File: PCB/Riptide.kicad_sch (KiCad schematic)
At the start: 180 parts, among them SW1 SW_Push, SW10 SW_Push, SW11 SW_Push, SW12 SW_Push, SW13 SW_Push, SW14 SW_Push, SW15 SW_Push, SW16 SW_Push, SW17 SW_Push, SW18 SW_Push, SW19 SW_Push, SW2 SW_Push, SW20 SW_Push, SW21 SW_Push, SW22 SW_Push, SW23 SW_Push, SW24 SW_Push, SW25 SW_Push, SW26 SW_Push, SW27 SW_Push, SW28 SW_Push, SW29 SW_Push, SW3 SW_Push, SW30 SW_Push, SW31 SW_Push, SW32 SW_Push, SW33 SW_Push, SW34 SW_Push, SW35 SW_Push, SW36 SW_Push, SW37 SW_Push, SW38 SW_Push, SW39 SW_Push, SW4 SW_Push, SW40 SW_Push, SW41 SW_Push, SW42 SW_Push, SW43 SW_Push, SW44 SW_Push, SW45 SW_Push, SW46 SW_Push, SW47 SW_Push, SW48 SW_Push, SW49 SW_Push, SW5 SW_Push, SW50 SW_Push, SW51 SW_Push, SW52 SW_Push, SW53 SW_Push, SW54 SW_Push, SW55 SW_Push, SW56 SW_Push, SW57 SW_Push, SW58 SW_Push, SW59 SW_Push, SW6 SW_Push, SW60 SW_Push, SW61 SW_Push, SW62 SW_Push, SW63 SW_Push, SW64 SW_Push, SW65 SW_Push, SW66 SW_Push, SW67 SW_Push, SW68 SW_Push, SW69 SW_Push, SW7 SW_Push, SW70 SW_Push, SW71 SW_Push, SW72 SW_Push, SW73 SW_Push, SW74 SW_Push, SW75 SW_Push, SW76 SW_Push, SW77 SW_Push, SW78 SW_Push, SW79 SW_Push, SW8 SW_Push, SW80 SW_Push, SW81 SW_Push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

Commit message: Finally Done!!
I have been working on this off and on since the 1st lol
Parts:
- removed D63, D64, D65, D66, D67, D69, D70, D71, D72, D77, D78, D80, D81, D82, D83, D84, D86, D87, D88, D89, D90: D, symbol Device:D
- removed SW12, SW18, SW34, SW50, SW61, SW65, SW66, SW67, SW68, SW69, SW73, SW74, SW75, SW76, SW77, SW81, SW82, SW83, SW84, SW85, SW86, SW87, SW88, SW89, SW90: SW_Push, symbol Switch:SW_Push_45deg
- added A1: RaspberryPi_Pico, Module:RaspberryPi_Pico_Common_Unspecified, symbol MCU_Module:RaspberryPi_Pico
- added D102, D105, D106, D115, D116, D117, D118, D119, D120, D121, D122, D123, D124, D97, D98, D99: D, Diode_THT:D_DO-35_SOD27_P7.62mm_Horizontal, symbol Device:D
- added H1, H10, H11, H12, H13, H14, H2, H3, H4, H5, H6, H7, H8, H9: X6511FRS-05-C85D30, Custom:HDR-SMD_5P-P2.54-H-F_X6511FRS-19-C85D30, symbol LCSC Custom:X6511FRS-05-C85D30
- added LED1, LED10, LED11, LED12, LED13, LED14, LED15, LED16, LED17, LED18, LED19, LED2, LED20, LED21, LED22, LED23, LED24, LED25, LED26, LED27, LED28, LED29, LED3, LED30, LED31, LED32, LED33, LED34, LED35, LED36, LED37, LED38, LED39, LED4, LED40, LED41, LED42, LED43, LED44, LED45, LED46, LED47, LED48, LED49, LED5, LED50, LED51, LED52, LED53, LED54, LED55, LED56, LED57, LED58, LED59, LED6, LED60, LED61, LED7, LED8, LED9: SK6812MINI, Custom:LED_SK6812MINI_PLCC4_3.5x3.5mm_P1.75mm, symbol LED:SK6812MINI
- added R1, R2: 4.7K, Resistor_THT:R_Axial_DIN0204_L3.6mm_D1.6mm_P5.08mm_Horizontal, symbol Device:R
- added SW14, SW15, SW16, SW22, SW23, SW24, SW31, SW38, SW39, SW40, SW46, SW48, SW54, SW55, SW7, SW8: SW_Push, Custom Keyboard Parts:SW_Cherry_MX_PCB_1.00u, symbol Switch:SW_Push_45deg
- added SW30: SW_Push, Custom Keyboard Parts:SW_Cherry_MX_PCB_2.00u, symbol Switch:SW_Push_45deg
- added SW32: SW_Push, Custom Keyboard Parts:SW_Cherry_MX_PCB_1.50u, symbol Switch:SW_Push_45deg
- added SW47: SW_Push, Custom Keyboard Parts:SW_Cherry_MX_PCB_1.75u, symbol Switch:SW_Push_45deg
- added SW85: RotaryEncoder_Switch, Rotary_Encoder:RotaryEncoder_Alps_EC11E-Switch_Vertical_H20mm, symbol Device:RotaryEncoder_Switch
- added U1: PCA9555D, Package_SO:SOIC-24W_7.5x15.4mm_P1.27mm, symbol Interface_Expansion:PCA9555D
- added U2: ~, Custom:SSD1306-0.91-OLED-4pin-128x32, symbol Custom:Mini_OLED
- D1, D10, D11, D12, D13, D14, D15, D16, D17, D18, D19, D2, D20, D21, D22, D23, D24, D25, D26, D27, D28, D29, D3, D30, D31, D32, D33, D34, D35, D36, D37, D38, D39, D4, D40, D41, D42, D43, D44, D45, D46, D47, D48, D49, D5, D50, D51, D52, D53, D54, D55, D56, D57, D58, D59, D6, D60, D61, D62, D68, D7, D73, D74, D75, D76, D79, D8, D85, D9: footprint (none) -> Diode_THT:D_DO-35_SOD27_P7.62mm_Horizontal
- SW1, SW2, SW3, SW4, SW5, SW56, SW6, SW62, SW63, SW64, SW70, SW71, SW79, SW80: footprint (none) -> Custom Keyboard Parts:SW_Cherry_MX_PCB_1.00u
- SW10: renamed from SW8; footprint (none) -> Custom Keyboard Parts:SW_Cherry_MX_PCB_1.00u
- SW11: renamed from SW9; footprint (none) -> Custom Keyboard Parts:SW_Cherry_MX_PCB_1.00u
- SW12: renamed from SW10; footprint (none) -> Custom Keyboard Parts:SW_Cherry_MX_PCB_1.00u
- SW13: renamed from SW11; footprint (none) -> Custom Keyboard Parts:SW_Cherry_MX_PCB_1.00u
- SW17: renamed from SW13; footprint (none) -> Custom Keyboard Parts:SW_Cherry_MX_PCB_1.00u
- SW18: renamed from SW14; footprint (none) -> Custom Keyboard Parts:SW_Cherry_MX_PCB_1.00u
- SW19: renamed from SW15; footprint (none) -> Custom Keyboard Parts:SW_Cherry_MX_PCB_1.00u
- SW20: renamed from SW16; footprint (none) -> Custom Keyboard Parts:SW_Cherry_MX_PCB_1.00u
- SW21: renamed from SW17; footprint (none) -> Custom Keyboard Parts:SW_Cherry_MX_PCB_1.00u
- SW25: renamed from SW19; footprint (none) -> Custom Keyboard Parts:SW_Cherry_MX_PCB_1.00u
- SW26: renamed from SW20; footprint (none) -> Custom Keyboard Parts:SW_Cherry_MX_PCB_1.00u
- SW27: renamed from SW21; footprint (none) -> Custom Keyboard Parts:SW_Cherry_MX_PCB_1.00u
- SW28: renamed from SW22; footprint (none) -> Custom Keyboard Parts:SW_Cherry_MX_PCB_1.00u
- SW29: renamed from SW23; footprint (none) -> Custom Keyboard Parts:SW_Cherry_MX_PCB_1.00u
- SW33: renamed from SW24; footprint (none) -> Custom Keyboard Parts:SW_Cherry_MX_PCB_1.00u
- SW34: renamed from SW25; footprint (none) -> Custom Keyboard Parts:SW_Cherry_MX_PCB_1.00u
- SW35: renamed from SW26; footprint (none) -> Custom Keyboard Parts:SW_Cherry_MX_PCB_1.00u
- SW36: renamed from SW27; footprint (none) -> Custom Keyboard Parts:SW_Cherry_MX_PCB_1.00u
- SW37: renamed from SW28; footprint (none) -> Custom Keyboard Parts:SW_Cherry_MX_PCB_1.00u
- SW41: renamed from SW29; footprint (none) -> Custom Keyboard Parts:SW_Cherry_MX_PCB_1.00u
- SW42: renamed from SW30; footprint (none) -> Custom Keyboard Parts:SW_Cherry_MX_PCB_1.00u
- SW43: renamed from SW31; footprint (none) -> Custom Keyboard Parts:SW_Cherry_MX_PCB_1.00u
- SW44: renamed from SW32; footprint (none) -> Custom Keyboard Parts:SW_Cherry_MX_PCB_1.00u
- SW45: renamed from SW33; footprint (none) -> Custom Keyboard Parts:SW_Cherry_MX_PCB_1.50u
- SW49: renamed from SW35; footprint (none) -> Custom Keyboard Parts:SW_Cherry_MX_PCB_1.00u
- SW50: renamed from SW36; footprint (none) -> Custom Keyboard Parts:SW_Cherry_MX_PCB_1.00u
- SW51: renamed from SW37; footprint (none) -> Custom Keyboard Parts:SW_Cherry_MX_PCB_1.00u
- SW52: renamed from SW38; footprint (none) -> Custom Keyboard Parts:SW_Cherry_MX_PCB_1.00u
- SW53: renamed from SW39; footprint (none) -> Custom Keyboard Parts:SW_Cherry_MX_PCB_1.00u
- SW57: renamed from SW40; footprint (none) -> Custom Keyboard Parts:SW_Cherry_MX_PCB_1.00u
- SW58: renamed from SW41; footprint (none) -> Custom Keyboard Parts:SW_Cherry_MX_PCB_1.00u
- SW59: renamed from SW42; footprint (none) -> Custom Keyboard Parts:SW_Cherry_MX_PCB_2.25u
- SW60: renamed from SW43; footprint (none) -> Custom Keyboard Parts:SW_Cherry_MX_PCB_1.00u
- SW61: renamed from SW44; footprint (none) -> Custom Keyboard Parts:SW_Cherry_MX_PCB_2.25u
- SW65: renamed from SW45; footprint (none) -> Custom Keyboard Parts:SW_Cherry_MX_PCB_1.00u
- SW66: renamed from SW46; footprint (none) -> Custom Keyboard Parts:SW_Cherry_MX_PCB_1.00u
- SW67: renamed from SW47; footprint (none) -> Custom Keyboard Parts:SW_Cherry_MX_PCB_1.00u
- SW68: renamed from SW48; footprint (none) -> Custom Keyboard Parts:SW_Cherry_MX_PCB_1.00u
- SW69: renamed from SW49; footprint (none) -> Custom Keyboard Parts:SW_Cherry_MX_PCB_1.00u
- SW72: footprint (none) -> Custom Keyboard Parts:SW_Cherry_MX_PCB_1.75u
- SW73: renamed from SW51; footprint (none) -> Custom Keyboard Parts:SW_Cherry_MX_PCB_1.00u
- SW74: renamed from SW52; footprint (none) -> Custom Keyboard Parts:SW_Cherry_MX_PCB_1.00u
- SW75: renamed from SW53; footprint (none) -> Custom Keyboard Parts:SW_Cherry_MX_PCB_1.25u
- SW76: renamed from SW54; footprint (none) -> Custom Keyboard Parts:SW_Cherry_MX_PCB_1.25u
- SW77: renamed from SW55; footprint (none) -> Custom Keyboard Parts:SW_Cherry_MX_PCB_1.25u
- SW78: footprint (none) -> Custom Keyboard Parts:SW_Cherry_MX_6.25u_PCB
- SW81: renamed from SW57; footprint (none) -> Custom Keyboard Parts:SW_Cherry_MX_PCB_1.00u
- SW82: renamed from SW58; footprint (none) -> Custom Keyboard Parts:SW_Cherry_MX_PCB_1.00u
- SW83: renamed from SW59; footprint (none) -> Custom Keyboard Parts:SW_Cherry_MX_PCB_1.00u
- SW84: renamed from SW60; footprint (none) -> Custom Keyboard Parts:SW_Cherry_MX_PCB_1.00u
- SW9: renamed from SW7; footprint (none) -> Custom Keyboard Parts:SW_Cherry_MX_PCB_1.00u
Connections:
- net Column 11 is gone; now on net Column 7: SW63.1, SW64.1
- net Column 12 is gone; now on net Column 8: SW70.1, SW71.1, SW72.1
- net Column 13 is gone; now on net Column 9: SW78.1, SW79.1
- net Column 14 is gone; now on net Column 9: SW80.1
- net Column 0: now also A1.4 (GPIO2), SW7.1, SW8.1
- net Column 1: now also A1.5 (GPIO3), SW14.1, SW15.1, SW16.1
- net Column 10: now also A1.16 (GPIO12), SW85.S1; no longer SW62.1
- net Column 2: now also A1.6 (GPIO4), SW22.1, SW23.1, SW24.1
- net Column 3: now also A1.7 (GPIO5), SW30.1, SW31.1, SW32.1
- net Column 4: now also A1.9 (GPIO6), SW38.1, SW39.1, SW40.1
- net Column 5: now also A1.10 (GPIO7), SW46.1, SW47.1, SW48.1
- net Column 6: now also SW56.1, A1.11 (GPIO8), SW54.1, SW55.1
- net Column 7: now also SW62.1, A1.12 (GPIO9)
- net Column 8: now also A1.14 (GPIO10)
- net Column 9: now also A1.15 (GPIO11); no longer SW56.1
- net Row 0: now also A1.17 (GPIO13); no longer D74.1 (K)
- net Row 1: now also A1.19 (GPIO14); no longer D75.1 (K)
- net Row 2: now also A1.20 (GPIO15); no longer D76.1 (K)
- net Row 4: now also A1.22 (GPIO17); no longer D73.1 (K)
- net Row 5: now also A1.24 (GPIO18)
- net at SW56.2: now also D121.2 (A); no longer D56.2 (A)
- net at SW80.2: now also D124.2 (A)
- net at D75.2 (A): now also SW55.2
- net Encoder SW 2: now reaches D61.2 (A)
- net Encoder SW 2: now also SW85.S2
- net at D12.2 (A): now also SW14.2
- net at SW78.2: now also D85.2 (A)
- net at SW64.2: now also D122.2 (A)
- net at D79.2 (A): now also SW70.2; no longer SW79.2
- net at SW71.2: now also D105.2 (A)
- net at SW62.2: now also D68.2 (A); no longer D62.2 (A)
- net at D34.2 (A): now also SW30.2
- net at SW63.2: now also D76.2 (A)
- net at SW72.2: now also D123.2 (A)
- net at D18.2 (A): now also SW22.2
- net at D74.2 (A): now also SW39.2
- net at D50.2 (A): now also SW38.2
- net at D73.2 (A): now also SW31.2
- net Column 15 renamed Row 3
- net Row 3: now also A1.21 (GPIO16)
- new net: LED55.1 (DOUT), LED56.3 (DIN)
- new net: LED54.1 (DOUT), LED55.3 (DIN)
- new net: D116.2 (A), SW16.2
- new net: D115.2 (A), SW8.2
- new net: LED12.1 (DOUT), LED13.3 (DIN)
- new net: LED11.1 (DOUT), LED12.3 (DIN)
- new net: LED60.1 (DOUT), LED61.3 (DIN)
- new net: D118.2 (A), SW32.2
- new net: LED45.1 (DOUT), LED46.3 (DIN)
- new net: LED44.1 (DOUT), LED45.3 (DIN)
- new net: LED43.1 (DOUT), LED44.3 (DIN)
- new net: LED41.1 (DOUT), LED42.3 (DIN)
- new net: LED40.1 (DOUT), LED41.3 (DIN)
- new net: LED37.1 (DOUT), LED38.3 (DIN)
- new net: LED36.1 (DOUT), LED37.3 (DIN)
- new net: LED13.1 (DOUT), LED14.3 (DIN)
- new net: D97.2 (A), SW7.2
- new net: LED47.1 (DOUT), LED48.3 (DIN)
- new net: LED46.1 (DOUT), LED47.3 (DIN)
- new net: D98.2 (A), SW15.2
- new net: LED7.1 (DOUT), LED8.3 (DIN)
- new net: LED6.1 (DOUT), LED7.3 (DIN)
- new net: LED35.1 (DOUT), LED36.3 (DIN)
- new net: LED34.1 (DOUT), LED35.3 (DIN)
- new net: LED50.1 (DOUT), LED51.3 (DIN)
- new net: LED49.1 (DOUT), LED50.3 (DIN)
- new net: D102.2 (A), SW47.2
- new net: LED5.1 (DOUT), LED6.3 (DIN)
- new net: LED30.1 (DOUT), LED31.3 (DIN)
- new net: LED29.1 (DOUT), LED30.3 (DIN)
- new net: LED27.1 (DOUT), LED28.3 (DIN)
- new net: LED26.1 (DOUT), LED27.3 (DIN)
- new net: LED10.1 (DOUT), LED11.3 (DIN)
- new net: LED51.1 (DOUT), LED52.3 (DIN)
- new net: LED39.1 (DOUT), LED40.3 (DIN)
- new net: LED38.1 (DOUT), LED39.3 (DIN)
- new net: D117.2 (A), SW24.2
- new net: LED18.1 (DOUT), LED19.3 (DIN)
- new net: LED17.1 (DOUT), LED18.3 (DIN)
- new net: LED28.1 (DOUT), LED29.3 (DIN)
- new net: LED4.1 (DOUT), LED5.3 (DIN)
- new net: LED3.1 (DOUT), LED4.3 (DIN)
- new net: D120.2 (A), SW48.2
- new net: LED2.1 (DOUT), LED3.3 (DIN)
- new net: LED1.1 (DOUT), LED2.3 (DIN)
- new net: LED32.1 (DOUT), LED33.3 (DIN)
- new net: LED31.1 (DOUT), LED32.3 (DIN)
- new net: LED42.1 (DOUT), LED43.3 (DIN)
- new net: D62.2 (A), SW54.2
- new net: LED25.1 (DOUT), LED26.3 (DIN)
- new net: LED24.1 (DOUT), LED25.3 (DIN)
- new net: LED23.1 (DOUT), LED24.3 (DIN)
- new net: LED22.1 (DOUT), LED23.3 (DIN)
- new net: LED10.3 (DIN), LED9.1 (DOUT)
- new net: LED8.1 (DOUT), LED9.3 (DIN)
- new net: D119.2 (A), SW40.2
- new net: LED53.1 (DOUT), LED54.3 (DIN)
- new net: LED52.1 (DOUT), LED53.3 (DIN)
- new net: D106.2 (A), SW79.2
- new net: LED21.1 (DOUT), LED22.3 (DIN)
- new net: LED20.1 (DOUT), LED21.3 (DIN)
- new net: LED48.1 (DOUT), LED49.3 (DIN)
- new net: D99.2 (A), SW23.2
- new net: LED33.1 (DOUT), LED34.3 (DIN)
- new net: LED56.1 (DOUT), LED57.3 (DIN)
- new net: LED59.1 (DOUT), LED60.3 (DIN)
- new net: LED58.1 (DOUT), LED59.3 (DIN)
- new net: LED16.1 (DOUT), LED17.3 (DIN)
- new net: LED15.1 (DOUT), LED16.3 (DIN)
- new net: D56.2 (A), SW46.2
- new net: LED57.1 (DOUT), LED58.3 (DIN)
- new net: LED19.1 (DOUT), LED20.3 (DIN)
- new net +3.3V: A1.36 (3V3), R1.2, R2.2, U1.24 (VDD), U2.2 (VCC)
- new net +5V: A1.40 (VBUS), H1.1 (5V), H10.1 (5V), H11.1 (5V), H12.1 (5V), H13.1 (5V), H14.1 (5V), H2.1 (5V), H3.1 (5V), H4.1 (5V), H5.1 (5V), H6.1 (5V), H7.1 (5V), H8.1 (5V), H9.1 (5V), LED1.4 (VDD), LED10.4 (VDD), LED11.4 (VDD), LED12.4 (VDD), LED13.4 (VDD), LED14.4 (VDD), LED15.4 (VDD), LED16.4 (VDD), LED17.4 (VDD), LED18.4 (VDD), LED19.4 (VDD), LED2.4 (VDD), LED20.4 (VDD), LED21.4 (VDD), LED22.4 (VDD), LED23.4 (VDD), LED24.4 (VDD), LED25.4 (VDD), LED26.4 (VDD), LED27.4 (VDD), LED28.4 (VDD), LED29.4 (VDD), LED3.4 (VDD), LED30.4 (VDD), LED31.4 (VDD), LED32.4 (VDD), LED33.4 (VDD), LED34.4 (VDD), LED35.4 (VDD), LED36.4 (VDD), LED37.4 (VDD), LED38.4 (VDD), LED39.4 (VDD), LED4.4 (VDD), LED40.4 (VDD), LED41.4 (VDD), LED42.4 (VDD), LED43.4 (VDD), LED44.4 (VDD), LED45.4 (VDD), LED46.4 (VDD), LED47.4 (VDD), LED48.4 (VDD), LED49.4 (VDD), LED5.4 (VDD), LED50.4 (VDD), LED51.4 (VDD), LED52.4 (VDD), LED53.4 (VDD), LED54.4 (VDD), LED55.4 (VDD), LED56.4 (VDD), LED57.4 (VDD), LED58.4 (VDD), LED59.4 (VDD), LED6.4 (VDD), LED60.4 (VDD), LED61.4 (VDD), LED7.4 (VDD), LED8.4 (VDD), LED9.4 (VDD)
- new net EN 1: H1.2 (EN), U1.4 (IO0_0)
- new net EN 10: H10.2 (EN), U1.14 (IO1_1)
- new net EN 11: H11.2 (EN), U1.15 (IO1_2)
- new net EN 12: H12.2 (EN), U1.16 (IO1_3)
- new net EN 13: H13.2 (EN), U1.17 (IO1_4)
- new net EN 14: H14.2 (EN), U1.18 (IO1_5)
- new net EN 2: H2.2 (EN), U1.5 (IO0_1)
- new net EN 3: H3.2 (EN), U1.6 (IO0_2)
- new net EN 4: H4.2 (EN), U1.7 (IO0_3)
- new net EN 5: H5.2 (EN), U1.8 (IO0_4)
- new net EN 6: H6.2 (EN), U1.9 (IO0_5)
- new net EN 7: H7.2 (EN), U1.10 (IO0_6)
- new net EN 8: H8.2 (EN), U1.11 (IO0_7)
- new net EN 9: H9.2 (EN), U1.13 (IO1_0)
- new net Encoder A: A1.27 (GPIO21), SW85.A
- new net Encoder B: A1.29 (GPIO22), SW85.B
- new net GND: A1.13 (GND), A1.18 (GND), A1.23 (GND), A1.28 (GND), A1.3 (GND), A1.38 (GND), A1.8 (GND), H1.3 (GND), H10.3 (GND), H11.3 (GND), H12.3 (GND), H13.3 (GND), H14.3 (GND), H2.3 (GND), H3.3 (GND), H4.3 (GND), H5.3 (GND), H6.3 (GND), H7.3 (GND), H8.3 (GND), H9.3 (GND), LED1.2 (VSS), LED10.2 (VSS), LED11.2 (VSS), LED12.2 (VSS), LED13.2 (VSS), LED14.2 (VSS), LED15.2 (VSS), LED16.2 (VSS), LED17.2 (VSS), LED18.2 (VSS), LED19.2 (VSS), LED2.2 (VSS), LED20.2 (VSS), LED21.2 (VSS), LED22.2 (VSS), LED23.2 (VSS), LED24.2 (VSS), LED25.2 (VSS), LED26.2 (VSS), LED27.2 (VSS), LED28.2 (VSS), LED29.2 (VSS), LED3.2 (VSS), LED30.2 (VSS), LED31.2 (VSS), LED32.2 (VSS), LED33.2 (VSS), LED34.2 (VSS), LED35.2 (VSS), LED36.2 (VSS), LED37.2 (VSS), LED38.2 (VSS), LED39.2 (VSS), LED4.2 (VSS), LED40.2 (VSS), LED41.2 (VSS), LED42.2 (VSS), LED43.2 (VSS), LED44.2 (VSS), LED45.2 (VSS), LED46.2 (VSS), LED47.2 (VSS), LED48.2 (VSS), LED49.2 (VSS), LED5.2 (VSS), LED50.2 (VSS), LED51.2 (VSS), LED52.2 (VSS), LED53.2 (VSS), LED54.2 (VSS), LED55.2 (VSS), LED56.2 (VSS), LED57.2 (VSS), LED58.2 (VSS), LED59.2 (VSS), LED6.2 (VSS), LED60.2 (VSS), LED61.2 (VSS), LED7.2 (VSS), LED8.2 (VSS), LED9.2 (VSS), SW85.C, U1.12 (VSS), U2.1 (GND)
- new net LED Glow Data: A1.32 (GPIO27_ADC1), LED15.3 (DIN)
- new net LED Indicator Data: A1.31 (GPIO26_ADC0), LED1.3 (DIN)
- new net Row 6: A1.25 (GPIO19), D102.1 (K), D105.1 (K), D106.1 (K), D73.1 (K), D74.1 (K), D75.1 (K), D76.1 (K), D97.1 (K), D98.1 (K), D99.1 (K)
- new net Row 7: A1.26 (GPIO20), D115.1 (K), D116.1 (K), D117.1 (K), D118.1 (K), D119.1 (K), D120.1 (K), D121.1 (K), D122.1 (K), D123.1 (K), D124.1 (K)
- new net SCL: A1.2 (GPIO1), H1.5 (SCL), H10.5 (SCL), H11.5 (SCL), H12.5 (SCL), H13.5 (SCL), H14.5 (SCL), H2.5 (SCL), H3.5 (SCL), H4.5 (SCL), H5.5 (SCL), H6.5 (SCL), H7.5 (SCL), H8.5 (SCL), H9.5 (SCL), R1.1, U1.22 (SCL), U2.3 (SCL)
- new net SDA: A1.1 (GPIO0), H1.4 (SDA), H10.4 (SDA), H11.4 (SDA), H12.4 (SDA), H13.4 (SDA), H14.4 (SDA), H2.4 (SDA), H3.4 (SDA), H4.4 (SDA), H5.4 (SDA), H6.4 (SDA), H7.4 (SDA), H8.4 (SDA), H9.4 (SDA), R2.1, U1.23 (SDA), U2.4 (SDA)
- no-connect marks 0 -> 12
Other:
- note added: "CONTROL"
- note added: "I2C BUS"
- note added: "INPUT"
- note added: "LEDS"
- title: Riptide -> Riptide Keyboard
- moved on the sheet: D1, D10, D11, D13, D14, D15, D16, D17, D19, D2, D20, D21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

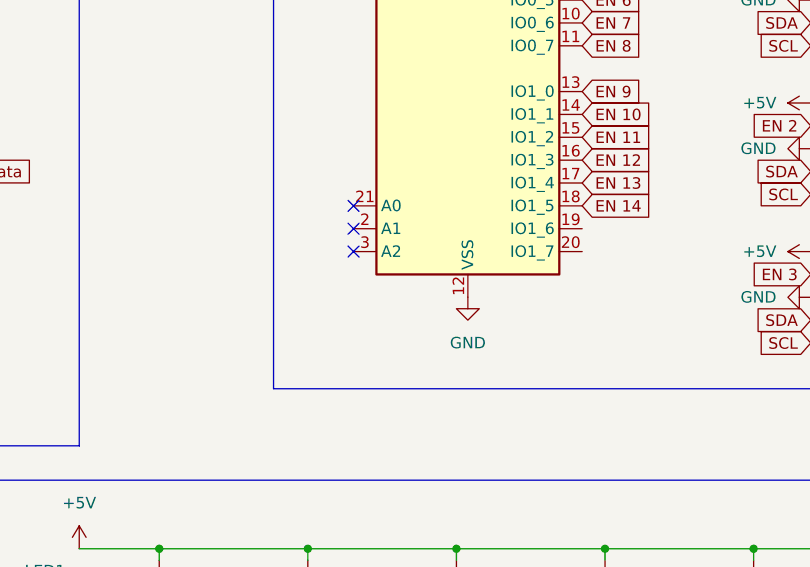
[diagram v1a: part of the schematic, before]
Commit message: Quick I2C Fix
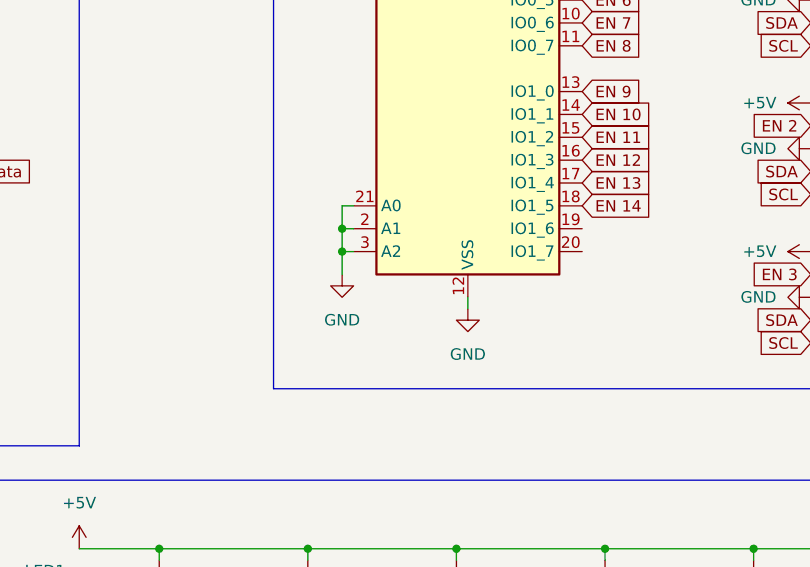
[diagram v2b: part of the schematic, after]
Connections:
- net GND: now also U1.2 (A1), U1.21 (A0), U1.3 (A2)
- no-connect marks 12 -> 9
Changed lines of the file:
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@@
 	)
 	(junction
+		(at 260.35 78.74)
+		(diameter 0)
+		(color 0 0 0 0)
+	)
+	(junction
 		(at 240.03 238.76)
 		(diameter 0)
@@
 	)
 	(junction
+		(at 260.35 81.28)
+		(diameter 0)
+		(color 0 0 0 0)
+	)
+	(junction
 		(at 69.85 43.18)
 		(diameter 0)
@@
 	)
 	(no_connect
-		(at 261.62 76.2)
-	)
-	(no_connect
 		(at 331.47 140.97)
 	)
 	(no_connect
-		(at 261.62 78.74)
-	)
-	(no_connect
 		(at 179.07 21.59)
 	)
@@
 		(at 161.29 39.37)
 	)
-	(no_connect
-		(at 261.62 81.28)
-	)
 	(wire
 		(pts
@@
 	(wire
 		(pts
+			(xy 260.35 78.74) (xy 261.62 78.74)
+		)
+		(stroke
+			(width 0)
+			(type default)
+		)
+	)
+	(wire
+		(pts
 			(xy 313.69 158.75) (xy 314.96 158.75)
 		)
@@
 	(wire
 		(pts
+			(xy 274.32 87.63) (xy 274.32 86.36)
+		)
+		(stroke
+			(width 0)
+			(type default)
+		)
+	)
+	(wire
+		(pts
 			(xy 96.52 124.46) (xy 96.52 144.78)
 		)
@@
 	(wire
 		(pts
+			(xy 260.35 78.74) (xy 260.35 76.2)
+		)
+		(stroke
+			(width 0)
+			(type default)
+		)
+	)
+	(wire
+		(pts
 			(xy 339.09 219.71) (xy 339.09 220.98)
 		)
@@
 	(wire
 		(pts
+			(xy 260.35 81.28) (xy 261.62 81.28)
+		)
+		(stroke
+			(width 0)
+			(type default)
+		)
+	)
+	(wire
+		(pts
 			(xy 289.56 185.42) (xy 289.56 186.69)
 		)
@@
 	(wire
 		(pts
+			(xy 260.35 81.28) (xy 260.35 78.74)
+		)
+		(stroke
+			(width 0)
+			(type default)
+		)
+	)
+	(wire
+		(pts
 			(xy 364.49 140.97) (xy 363.22 140.97)
 		)
@@
 	(wire
 		(pts
+			(xy 260.35 76.2) (xy 261.62 76.2)
+		)
+		(stroke
+			(width 0)
+			(type default)
+		)
+	)
+	(wire
+		(pts
 			(xy 306.07 149.86) (xy 289.56 149.86)
 		)
@@
 	(wire
 		(pts
+			(xy 260.35 83.82) (xy 260.35 81.28)
+		)
+		(stroke
+			(width 0)
+			(type default)
+		)
+	)
+	(wire
+		(pts
 			(xy 52.07 124.46) (xy 52.07 144.78)
 		)
@@
 	)
 	(symbol
+		(lib_id "power:GND")
+		(at 260.35 83.82 0)
+		(unit 1)
+		(exclude_from_sim no)
+		(in_bom yes)
+		(on_board yes)
+		(dnp no)
+		(fields_autoplaced yes)
+		(property "Reference" "#PWR047"
+			(at 260.35 90.17 0)
+			(effects
+				(font
+					(size 1.27 1.27)
+				)
+				(hide yes)
+			)
+		)
+		(property "Value" "GND"
+			(at 260.35 88.9 0)
+			(effects
+				(font
+					(size 1.27 1.27)
+				)
+			)
+		)
+		(property "Footprint" ""
+			(at 260.35 83.82 0)
+			(effects
+				(font
+					(size 1.27 1.27)
+				)
+				(hide yes)
+			)
+		)
+		(property "Datasheet" ""
+			(at 260.35 83.82 0)
+			(effects
+				(font
+					(size 1.27 1.27)
+				)
+				(hide yes)
+			)
+		)
+		(property "Description" "Power symbol creates a global label with name \"GND\" , ground"
+			(at 260.35 83.82 0)
+			(effects
+				(font
+					(size 1.27 1.27)
+				)
+				(hide yes)
+			)
+		)
+		(pin "1"
+		)
+		(instances
+			(project "Riptide"
+				(path "/42ad2eac-87aa-4f76-ad34-3c7d12cec721"
+					(reference "#PWR047")
+					(unit 1)
+				)
+			)
+		)
+	)
+	(symbol
 		(lib_id "Switch:SW_Push_45deg")
 		(at 107.95 66.04 0)
@@
 	(symbol
 		(lib_id "power:GND")
-		(at 274.32 86.36 0)
+		(at 274.32 87.63 0)
 		(unit 1)
 		(exclude_from_sim no)
@@
 		(fields_autoplaced yes)
 		(property "Reference" "#PWR043"
-			(at 274.32 92.71 0)
+			(at 274.32 93.98 0)
 			(effects
 				(font
@@
 		)
 		(property "Value" "GND"
-			(at 274.32 91.44 0)
+			(at 274.32 92.71 0)
 			(effects
 				(font
@@
 		)
 		(property "Footprint" ""
-			(at 274.32 86.36 0)
+			(at 274.32 87.63 0)
 			(effects
 				(font
@@
 		)
 		(property "Datasheet" ""
-			(at 274.32 86.36 0)
+			(at 274.32 87.63 0)
 			(effects
 				(font
@@
 		)
 		(property "Description" "Power symbol creates a global label with name \"GND\" , ground"
-			(at 274.32 86.36 0)
+			(at 274.32 87.63 0)
 			(effects
 				(font
